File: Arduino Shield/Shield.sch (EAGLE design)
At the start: 5 parts

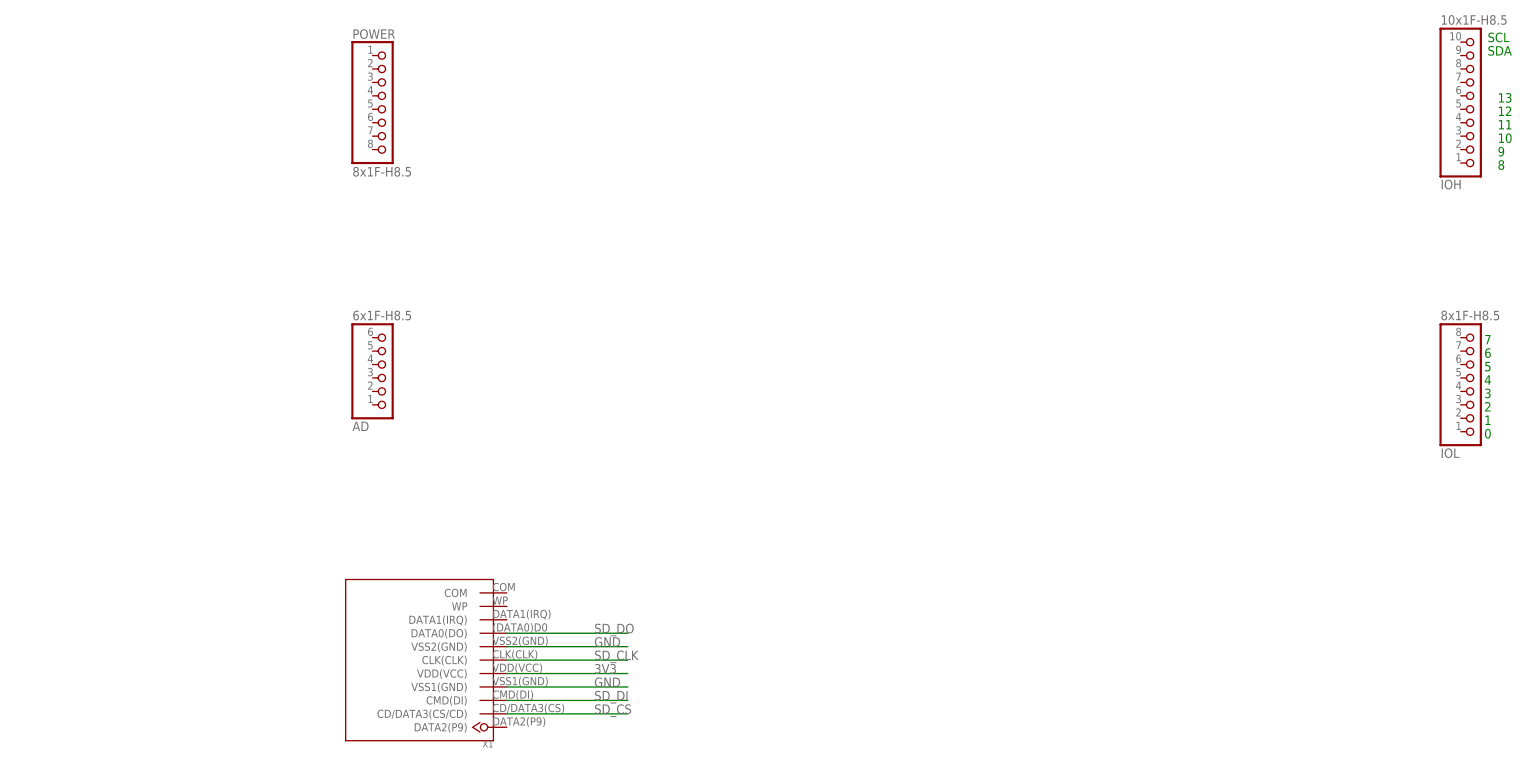
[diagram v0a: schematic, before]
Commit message: Schem of shield
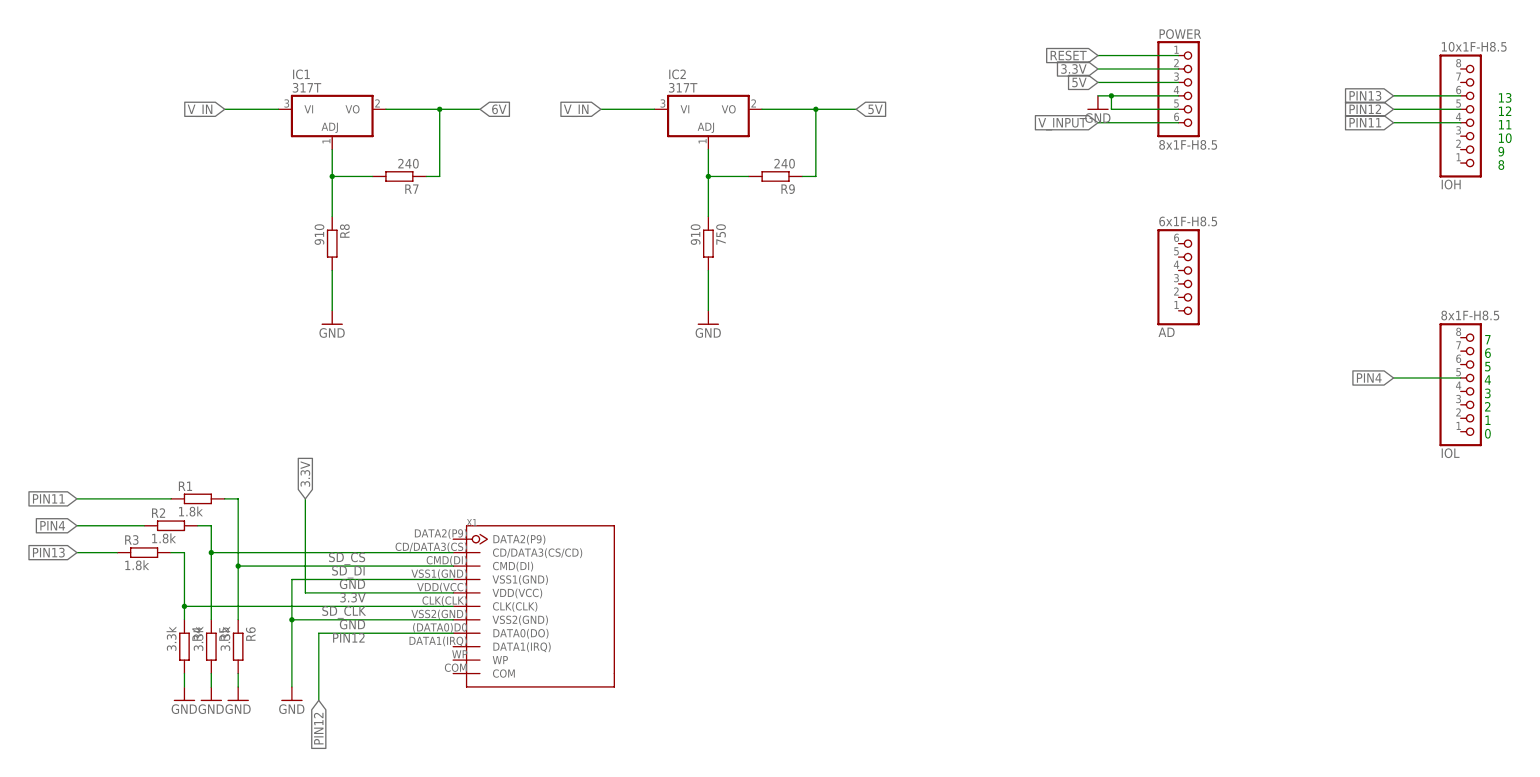
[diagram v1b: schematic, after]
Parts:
- added 750, R8: 910, resistor:R-EU_R0805
- added IC1, IC2: 317T, linear:317T
- added R1, R2, R3: 1.8k, resistor:R-EU_R0805
- added R4, R5, R6: 3.3k, resistor:R-EU_R0805
- added R7, R9: 240, resistor:R-EU_R0805
- IOH: device SmartPrj:PINHD-1X10_ARD -> pinhead:PINHD-1X8
- POWER: device SmartPrj:PINHD-1X8 -> pinhead:PINHD-1X6
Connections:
- removed net 3V3: X1.VDD(VCC)
- removed net SD_DO: X1.DATA0(DO)
- new net 3.3V: POWER.2, X1.VDD(VCC)
- new net 5V: IC2.VO, POWER.3, R9.1
- new net 6V: IC1.VO, R7.1
- new net N$1: IC1.ADJ, R7.2, R8.1
- new net N$2: 750.1, IC2.ADJ, R9.2
- new net PIN11: IOH.4, R1.1
- new net PIN12: IOH.5, X1.DATA0(DO)
- new net PIN13: IOH.6, R3.1
- new net PIN4: IOL.5, R2.1
- new net RESET: POWER.1
- new net V_IN: IC1.VI, IC2.VI
- new net V_INPUT: POWER.6
- net GND: now also 750.2, POWER.4, POWER.5, R4.2, R5.2, R6.2, R8.2
- net SD_CLK: now also R3.2, R4.1
- net SD_CS: now also R2.2, R5.1
- net SD_DI: now also R1.2, R6.1
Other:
- note removed: "SCL"
- note removed: "SDA"
- moved on the sheet: AD, X1
